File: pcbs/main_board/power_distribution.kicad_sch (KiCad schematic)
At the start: 3 parts, among them J1 BAT1, J2 BAT2, SW1 Power switch

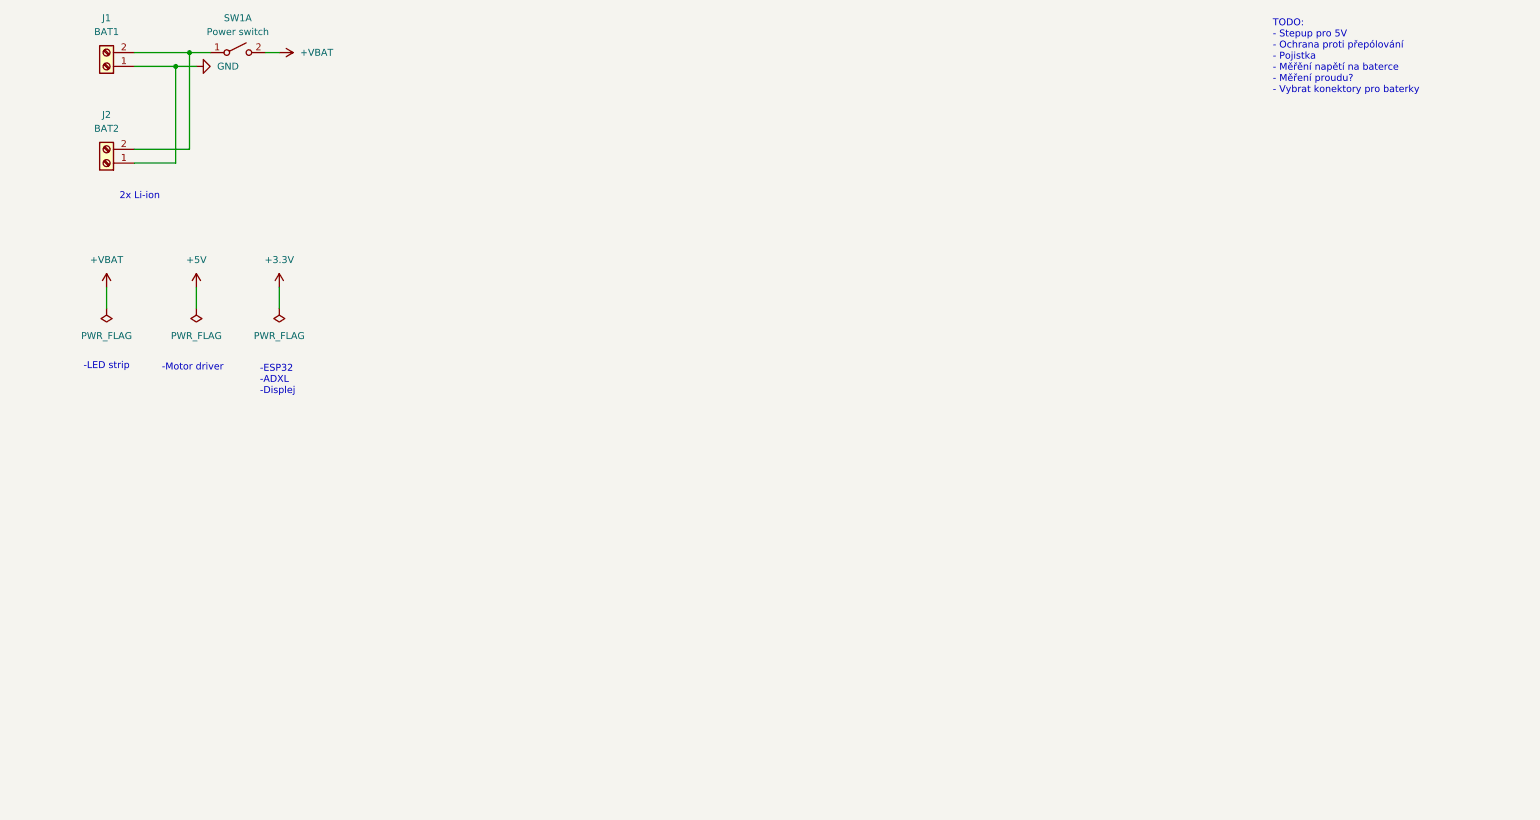
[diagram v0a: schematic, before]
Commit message: Add step-up into project
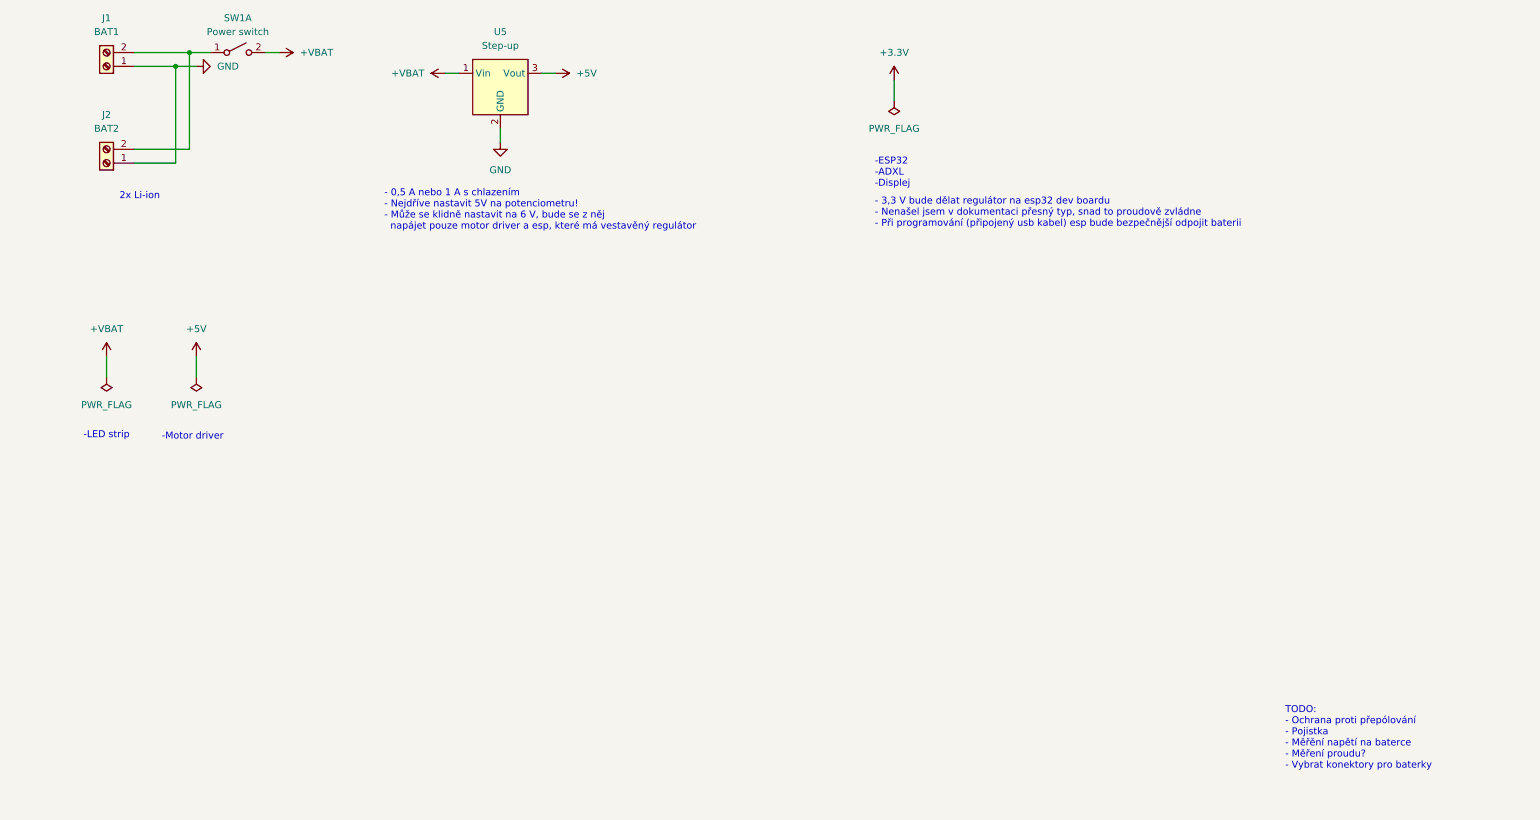
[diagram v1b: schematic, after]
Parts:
- added U5: Step-up, step-up_module:step-up_module, symbol step-up_module:_1
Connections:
- net +5V: now also U5.3 (Vout)
- net +VBAT: now also U5.1 (Vin)
- net GND: now also U5.2 (GND)
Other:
- note added: "- 0,5 A nebo 1 A s chlazením - Nejdříve nastavit 5V na potenciometru! - Může se klidně nastavit na 6 V, bude se z něj napájet pouze motor driver a esp, které má vestavěný regulátor"
- note added: "- 3,3 V bude dělat regulátor na esp32 dev boardu - Nenašel jsem v dokumentaci přesný typ, snad to proudově zvládne - Při programování (připojený usb kabel) esp bude bezpečnější odpojit baterii"
- note added: "TODO: - Ochrana proti přepólování - Pojistka - Měřění napětí na baterce - Měření proudu? - Vybrat konektory pro baterky"
- note removed: "TODO: - Stepup pro 5V - Ochrana proti přepólování - Pojistka - Měřění napětí na baterce - Měření proudu? - Vybrat konektory pro baterky"

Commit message: Add ideal diode
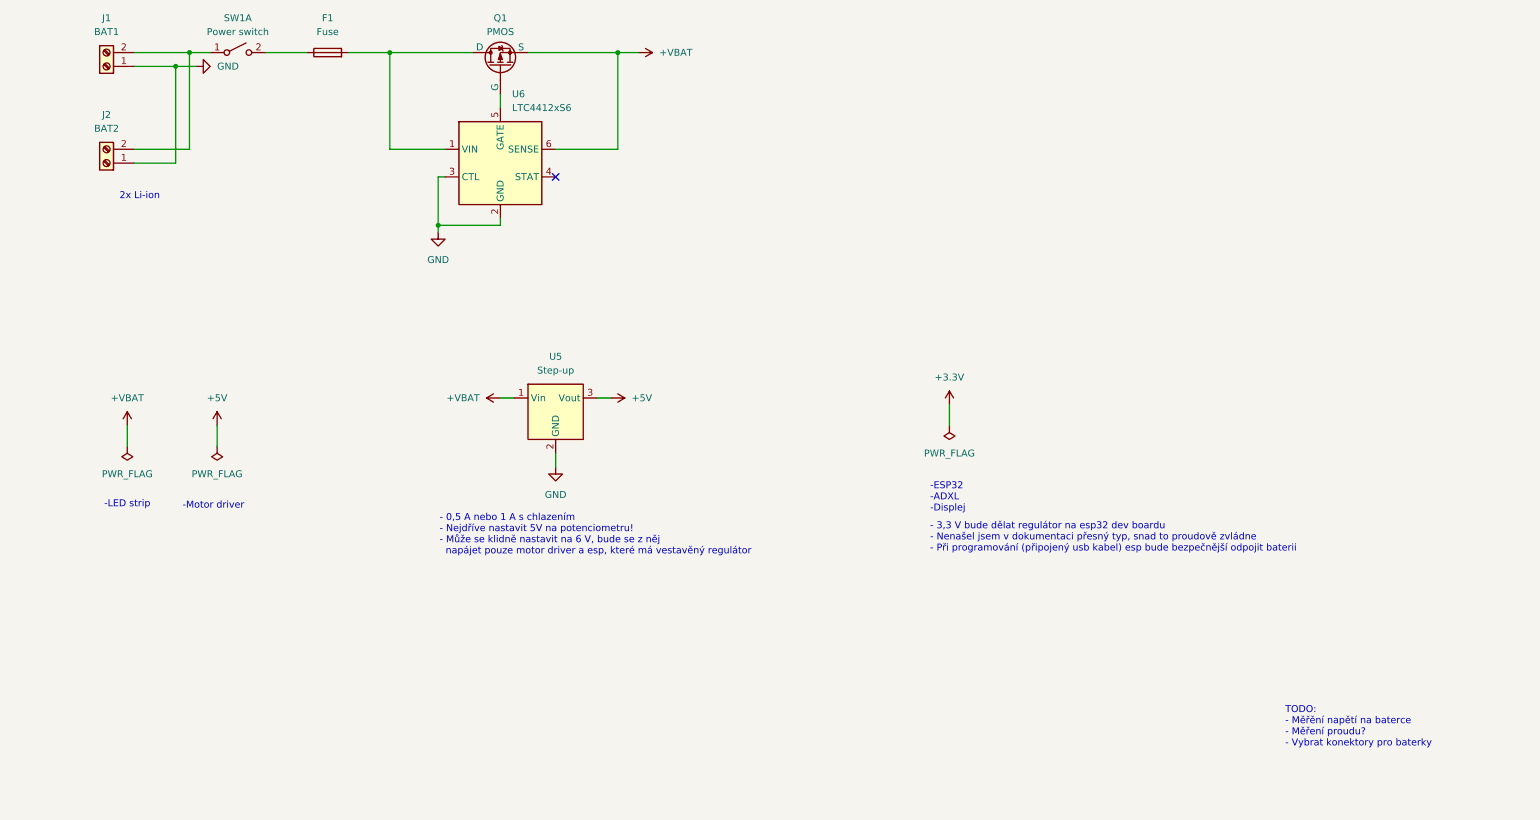
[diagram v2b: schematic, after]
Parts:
- added F1: Fuse, symbol Device:Fuse
- added Q1: PMOS, Package_TO_SOT_SMD:TO-252-2, symbol Simulation_SPICE:PMOS
- added U6: LTC4412xS6, Package_TO_SOT_SMD:TSOT-23-6, symbol Power_Management:LTC4412xS6
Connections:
- net +VBAT: now also Q1.3 (S), U6.6 (SENSE); no longer SW1.2 (B)
- net GND: now also U6.2 (GND), U6.3 (CTL)
- new net: F1.2, Q1.1 (D), U6.1 (VIN)
- new net: Q1.2 (G), U6.5 (GATE)
- new net: F1.1, SW1.2 (B)
- no-connect marks 0 -> 1
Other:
- note added: "TODO: - Měřění napětí na baterce - Měření proudu? - Vybrat konektory pro baterky"
- note removed: "TODO: - Ochrana proti přepólování - Pojistka - Měřění napětí na baterce - Měření proudu? - Vybrat konektory pro baterky"
- moved on the sheet: U5

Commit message: Add reverse polarity protection
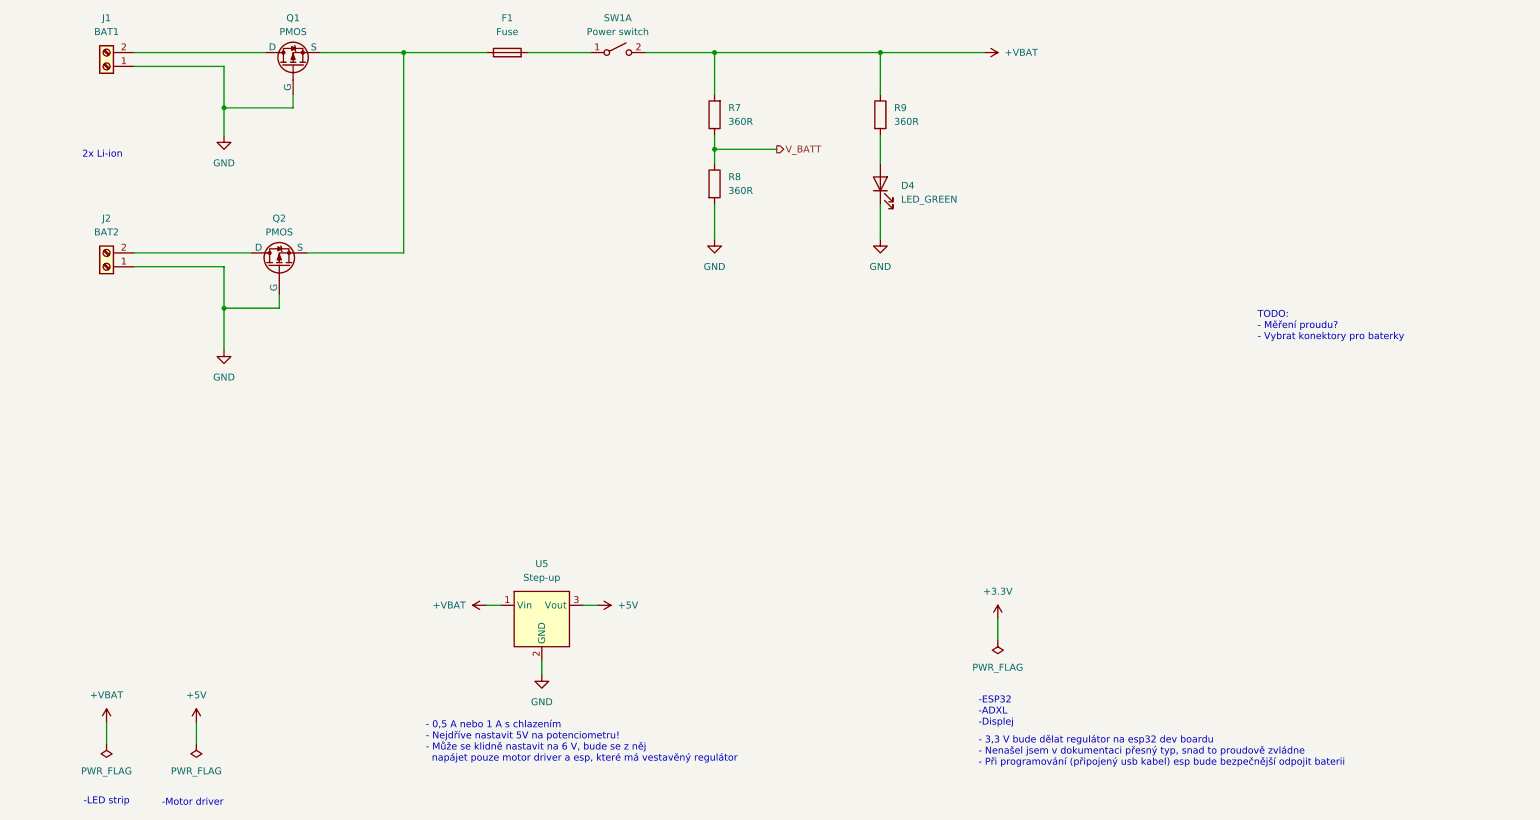
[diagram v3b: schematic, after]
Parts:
- removed U6: LTC4412xS6, Package_TO_SOT_SMD:TSOT-23-6, symbol Power_Management:LTC4412xS6
- added D4: LED_GREEN, LED_SMD:LED_0805_2012Metric_Pad1.15x1.40mm_HandSolder, symbol Device:LED
- added Q2: PMOS, Package_TO_SOT_SMD:TO-252-2, symbol Simulation_SPICE:PMOS
- added R7, R8, R9: 360R, Resistor_SMD:R_0603_1608Metric_Pad0.98x0.95mm_HandSolder, symbol Device:R
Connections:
- net +VBAT: now also SW1.2 (B), R7.2, R9.1; no longer Q1.3 (S)
- net GND: now also Q1.2 (G), D4.1 (K), Q2.2 (G), R8.2
- net at Q1.1 (D): now also J1.2 (Pin_2); no longer F1.2
- net at F1.1: now also Q1.3 (S), Q2.3 (S); no longer SW1.2 (B)
- new net: D4.2 (A), R9.2
- new net: F1.2, SW1.1 (A)
- new net: J2.2 (Pin_2), Q2.1 (D)
- new net V_BATT: R7.1, R8.1
- no-connect marks 1 -> 0
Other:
- note added: "TODO: - Měření proudu? - Vybrat konektory pro baterky"
- note removed: "TODO: - Měřění napětí na baterce - Měření proudu? - Vybrat konektory pro baterky"
- moved on the sheet: F1, J2, Q1, SW1A, U5

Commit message: Add connectors
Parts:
- removed Q2: PMOS, Package_TO_SOT_SMD:TO-252-2, symbol Simulation_SPICE:PMOS
- D4: value LED_GREEN -> POWER; Supplier (none) -> Mouser; Supplier Part Number (none) -> 604-APTD2012LCGCK; Ullmanna Part Number BMCLED102 -> (none)
- F1: value Fuse -> 5A
- J1, J2: footprint (none) -> Connector_JST:JST_XH_S2B-XH-A-1_1x02_P2.50mm_Horizontal; Manufacturer Part Number (none) -> S2B-XH-A-BK(LF)(SN); Supplier (none) -> Mouser; Supplier Part Number (none) -> 306-S2BXHABKLFSN
- R7: value 360R -> 22k; Manufacturer Part Number CRCW0603360RJNTA -> CRCW060322K0FKEBC; Supplier Part Number 71-CRCW0603J-360 -> 71-CRCW060322K0FKEBC
- R8: value 360R -> 68k; Manufacturer Part Number CRCW0603360RJNTA -> CRCW060368K0FKTA; Supplier Part Number 71-CRCW0603J-360 -> 71-CRCW0603-68K
- R9: value 360R -> 1k; Manufacturer Part Number CRCW0603360RJNTA -> CRCW06031K37FKEAHP; Supplier Part Number 71-CRCW0603J-360 -> 71-CRCW06031K37FKEAH
- SW1: footprint (none) -> Connector_JST:JST_XH_S4B-XH-A-1_1x04_P2.50mm_Horizontal; Manufacturer Part Number (none) -> S2B-XH-A-BK(LF)(SN); Supplier (none) -> Mouser; Supplier Part Number (none) -> 306-S2BXHABKLFSN
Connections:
- net +VBAT: now also F1.2; no longer SW1.2 (B)
- net at Q1.1 (D): now also SW1.2 (B); no longer J1.2 (Pin_2)
- net at SW1.1 (A): now also J1.2 (Pin_2), J2.2 (Pin_2); no longer F1.2
- net V_BATT renamed STATUS
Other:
- note added: "- 2x Li-ion - Není zde ochrana, pokud bude pouze jedna baterie přepólována"
- note added: "- 3,3 V bude dělat regulátor na esp32 dev boardu - Nenašel jsem v dokumentaci přesný typ, snad to proudově zvládne - Při programování přepojit propojku, napájení bude z usb"
- note added: "Dělič 22/68 -> 4.2V/3.173V"
- note added: "Ochrana proti přepólování a přetížení"
- note removed: "- 3,3 V bude dělat regulátor na esp32 dev boardu - Nenašel jsem v dokumentaci přesný typ, snad to proudově zvládne - Při programování (připojený usb kabel) esp bude bezpečnější odpojit baterii"
- note removed: "2x Li-ion"
- note removed: "TODO: - Měření proudu? - Vybrat konektory pro baterky"
- moved on the sheet: D4, F1, J2, Q1, R9, SW1A, U5

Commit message: ID pins, BOM, fuse
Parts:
- D4: Mouser Part Number 604-APTD2012LCGCK -> (none)
- F1: footprint (none) -> Fuse:Fuse_0603_1608Metric_Pad1.05x0.95mm_HandSolder; Manufacturer Part Number (none) -> SF-0603F500-2; Supplier (none) -> Mouser; Supplier Part Number (none) -> 652-SF-0603F500-2
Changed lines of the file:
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@@
-			)
-		)
-		(property "Mouser Part Number" "604-APTD2012LCGCK "
-			(at 189.23 53.34 0)
-			(effects
-				(font
-					(size 1.27 1.27)
-				)
-				(hide yes)
 			)
 		)
@@
 			)
 		)
-		(property "Footprint" ""
+		(property "Footprint" "Fuse:Fuse_0603_1608Metric_Pad1.05x0.95mm_HandSolder"
 			(at 118.11 30.988 90)
 			(effects
@@
 			)
 		)
-		(property "Datasheet" "~"
+		(property "Datasheet" "https://cz.mouser.com/datasheet/3/40/1/sf0603f.pdf"
 			(at 118.11 29.21 0)
 			(effects
@@
 			)
 		)
-		(property "Description" "Fuse"
+		(property "Description" "Fuse 5A"
 			(at 118.11 29.21 0)
 			(effects
 				(font
+					(size 1.27 1.27)
+				)
+				(hide yes)
+			)
+		)
+		(property "Manufacturer Part Number" "SF-0603F500-2"
+			(at 118.11 29.21 90)
+			(effects
+				(font
+					(size 1.27 1.27)
+				)
+				(hide yes)
+			)
+		)
+		(property "Supplier" "Mouser"
+			(at 118.11 29.21 90)
+			(effects
+				(font
+					(size 1.27 1.27)
+				)
+				(hide yes)
+			)
+		)
+		(property "Supplier Part Number" "652-SF-0603F500-2"
+			(at 118.11 29.21 90)
+			(effects
+				(font

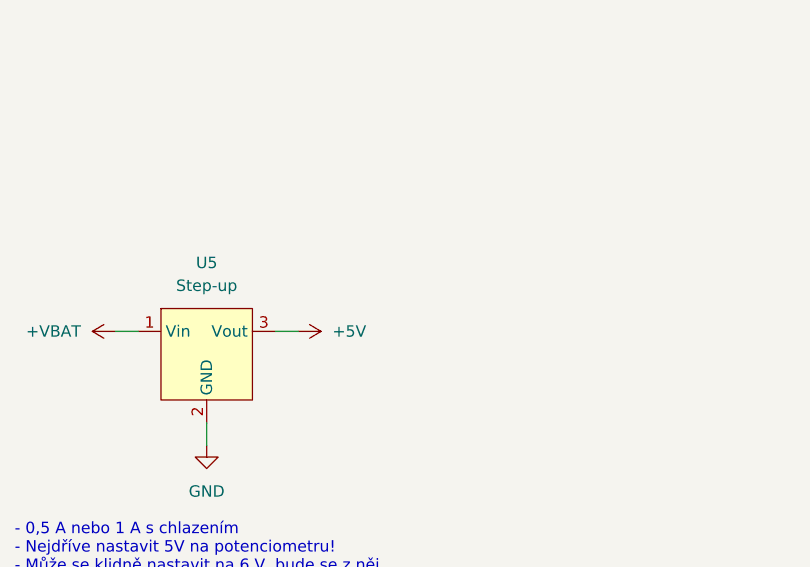
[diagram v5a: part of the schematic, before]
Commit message: ESP power update
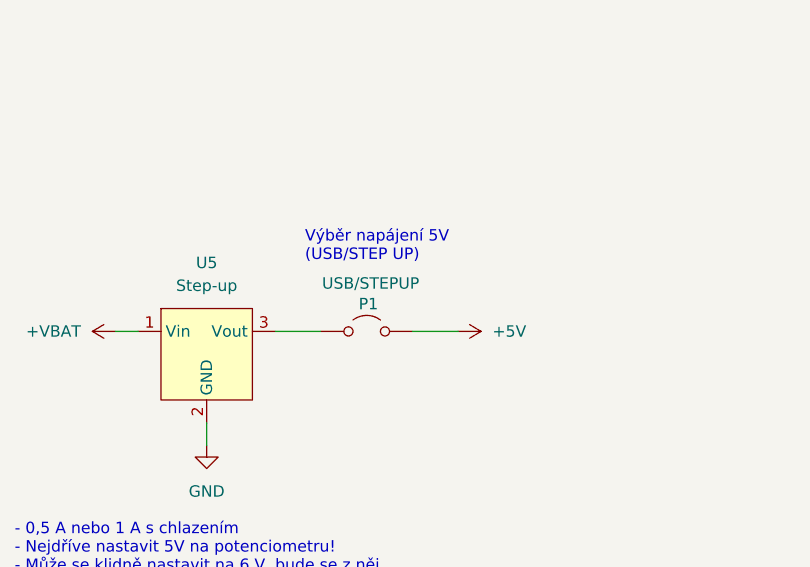
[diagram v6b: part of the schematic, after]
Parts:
- added P1: USB/STEPUP, Connector_PinHeader_2.54mm:PinHeader_1x03_P2.54mm_Horizontal, symbol Jumper:Jumper_2_Open
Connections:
- net +5V: now also P1.2 (B); no longer U5.3 (Vout)
- new net: P1.1 (A), U5.3 (Vout)
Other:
- note added: "Výběr napájení 5V (USB/STEP UP)"
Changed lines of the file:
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@@
+		)
+	)
+	(text "Výběr napájení 5V\n(USB/STEP UP)"
+		(exclude_from_sim no)
+		(at 136.652 104.394 0)
+		(effects
+			(font
+				(size 1.27 1.27)
+			)
+			(justify left top)
 		)
 	)
@@
 	(wire
 		(pts
-			(xy 133.35 115.57) (xy 135.89 115.57)
+			(xy 133.35 115.57) (xy 138.43 115.57)
 		)
 		(stroke
@@
 		(pts
 			(xy 143.51 44.45) (xy 143.51 46.99)
+		)
+		(stroke
+			(width 0)
+			(type default)
+		)
+	)
+	(wire
+		(pts
+			(xy 148.59 115.57) (xy 153.67 115.57)
 		)
 		(stroke
@@
 	(symbol
 		(lib_id "power:VCC")
-		(at 135.89 115.57 270)
+		(at 153.67 115.57 270)
 		(unit 1)
 		(exclude_from_sim no)
@@
 		(fields_autoplaced yes)
 		(property "Reference" "#PWR017"
-			(at 132.08 115.57 0)
+			(at 149.86 115.57 0)
 			(effects
 				(font
@@
 		)
 		(property "Value" "+5V"
-			(at 139.7 115.5699 90)
+			(at 157.48 115.5699 90)
 			(effects
 				(font
@@
 		)
 		(property "Footprint" ""
-			(at 135.89 115.57 0)
+			(at 153.67 115.57 0)
 			(effects
 				(font
@@
 		)
 		(property "Datasheet" ""
-			(at 135.89 115.57 0)
+			(at 153.67 115.57 0)
 			(effects
 				(font
@@
 		)
 		(property "Description" "Power symbol creates a global label with name \"VCC\""
-			(at 135.89 115.57 0)
+			(at 153.67 115.57 0)
 			(effects
 				(font
@@
 					(unit 1)
 				)
+			)
+		)
+	)
+	(symbol
+		(lib_id "Jumper:Jumper_2_Open")
+		(at 143.51 115.57 0)
+		(unit 1)
+		(exclude_from_sim no)
+		(in_bom yes)
+		(on_board yes)
+		(dnp no)
+		(property "Reference" "P1"
+			(at 144.78 112.522 0)
+			(effects
+				(font
+					(size 1.27 1.27)
+				)
+				(justify right)
+			)
+		)
+		(property "Value" "USB/STEPUP"
+			(at 149.352 110.236 0)
+			(effects
+				(font
+					(size 1.27 1.27)
+				)
+				(justify right)
+			)
+		)
+		(property "Footprint" "Connector_PinHeader_2.54mm:PinHeader_1x03_P2.54mm_Horizontal"
+			(at 143.51 115.57 0)
+			(effects
+				(font
+					(size 1.27 1.27)
+				)
+				(hide yes)
+			)
+		)
+		(property "Datasheet" "~"
+			(at 143.51 115.57 0)
+			(effects
+				(font
+					(size 1.27 1.27)
+				)
+				(hide yes)
+			)
+		)
+		(property "Description" "Kolíková lišta"
+			(at 143.51 115.57 0)
+			(effects
+				(font
+					(size 1.27 1.27)
+				)
+				(hide yes)
+			)
+		)
+		(property "Manufacturer Part Number" "LA217003A"
+			(at 143.51 115.57 90)
+			(effects
+				(font
+					(size 1.27 1.27)
+				)
+				(hide yes)
+			)
+		)
+		(property "Supplier" "LaskaKit"
+			(at 143.51 115.57 90)
+			(effects
+				(font
+					(size 1.27 1.27)
+				)
+				(hide yes)
+			)
+		)
+		(property "Supplier Part Number" "LA217003A"
+			(at 143.51 115.57 90)
+			(effects
+				(font
+					(size 1.27 1.27)
+				)
+				(hide yes)
+			)
+		)
+		(pin "2"
+		)
+		(pin "1"
+		)
+		(instances
+			(project "main_board"
+				(path "/86b00c07-962a-4c6d-8d05-813891e412c9/785d3379-347e-4437-9764-8387c52a78a7"
+					(reference "P1")
+					(unit 1)
+				)
